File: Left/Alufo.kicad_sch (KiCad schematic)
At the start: 27 parts, among them J1 USB_C_Receptacle_USB2.0_16P_2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, J3 USB_C_Receptacle_USB2.0_16P_2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, SW10 BOOT, U1 CH552T, U3 USBLC6-2P6, U5 USBLC6-2P6

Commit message: Remove status LED resistor
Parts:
- removed R9: 470R, Resistor_SMD:R_0805_2012Metric, symbol Device:R
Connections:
- net LED: now also L1.3 (DIN)
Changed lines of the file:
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@@
 	(wire
 		(pts
-			(xy 55.88 220.98) (xy 59.69 220.98)
-		)
-		(stroke
-			(width 0)
-			(type default)
-		)
-	)
-	(wire
-		(pts
 			(xy 132.08 43.18) (xy 134.62 43.18)
 		)
@@
 	(wire
 		(pts
-			(xy 67.31 220.98) (xy 69.85 220.98)
-		)
-		(stroke
-			(width 0)
-			(type default)
-		)
-	)
-	(wire
-		(pts
 			(xy 60.96 48.26) (xy 62.23 48.26)
 		)
@@
 	(global_label "LED"
 		(shape input)
-		(at 55.88 220.98 180)
+		(at 69.85 220.98 180)
 		(fields_autoplaced yes)
 		(effects
@@
 		)
 		(property "Intersheetrefs" "${INTERSHEET_REFS}"
-			(at 49.4477 220.98 0)
+			(at 63.4177 220.98 0)
 			(effects
 				(font
@@
 					(unit 1)
 				)
-			)
-		)
-	)
-	(symbol
-		(lib_id "Device:R")
-		(at 63.5 220.98 90)
-		(unit 1)
-		(exclude_from_sim no)
-		(in_bom yes)
-		(on_board yes)
-		(dnp no)
-		(property "Reference" "R9"
-			(at 63.5 216.408 90)
-			(effects
-				(font
-					(size 1.27 1.27)
-				)
-			)
-		)
-		(property "Value" "470R"
-			(at 63.5 218.948 90)
-			(effects
-				(font
-					(size 1.27 1.27)
-				)
-			)
-		)
-		(property "Footprint" "Resistor_SMD:R_0805_2012Metric"
-			(at 63.5 222.758 90)
-			(effects
-				(font
-					(size 1.27 1.27)
-				)
-				(hide yes)
-			)
-		)
-		(property "Datasheet" "~"
-			(at 63.5 220.98 0)
-			(effects
-				(font
-					(size 1.27 1.27)
-				)
-				(hide yes)
-			)
-		)
-		(property "Description" ""
-			(at 63.5 220.98 0)
-			(effects
-				(font
-					(size 1.27 1.27)
-				)
-				(hide yes)
-			)
-		)
-		(property "LCSC" "C23186"
-			(at 63.5 220.98 90)
-			(effects
-				(font
-					(size 1.27 1.27)
-				)
-				(hide yes)
-			)
-		)
-		(property "DigiKey" "311-5.10KHR"
-			(at 63.5 220.98 90)
-			(effects
-				(font
-					(size 1.27 1.27)
-				)
-				(hide yes)
-			)
-		)
-		(pin "1"
-		)
-		(pin "2"
-		)
-		(instances
-			(project "Alufo"
-				(path "/52f043ac-ccff-4c85-bc10-2db9d3c9e3f3"
-					(reference "R9")
-					(unit 1)
-				)

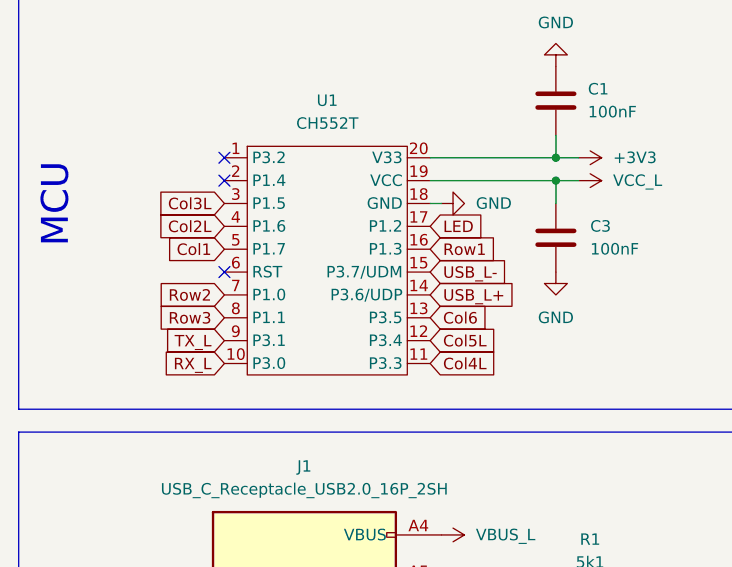
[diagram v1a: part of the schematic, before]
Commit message: Remove “L” from column labels
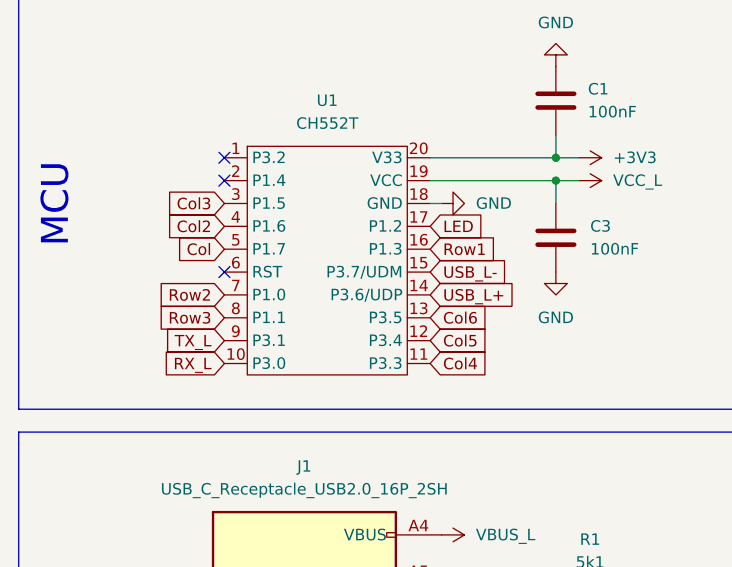
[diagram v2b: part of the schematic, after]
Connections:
- net Col1 renamed Col
- net Col2L renamed Col2
- net Col3L renamed Col3
- net Col4L renamed Col4
- net Col5L renamed Col5
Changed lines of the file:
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@@
 		)
 	)
-	(global_label "Col1"
+	(global_label "Col"
 		(shape input)
 		(at 38.1 53.34 180)
@@
 		)
 		(property "Intersheetrefs" "${INTERSHEET_REFS}"
-			(at 30.8211 53.34 0)
+			(at 32.0306 53.34 0)
 			(effects
 				(font
@@
 		)
 	)
-	(global_label "Col5L"
+	(global_label "Col5"
 		(shape input)
 		(at 60.96 63.5 0)
@@
 		)
 		(property "Intersheetrefs" "${INTERSHEET_REFS}"
-			(at 69.267 63.5 0)
+			(at 68.2389 63.5 0)
 			(effects
 				(font
@@
 		)
 	)
-	(global_label "Col3L"
+	(global_label "Col3"
 		(shape input)
 		(at 38.1 48.26 180)
@@
 		)
 		(property "Intersheetrefs" "${INTERSHEET_REFS}"
-			(at 29.793 48.26 0)
-			(effects
-				(font
-					(size 1.27 1.27)
-				)
-				(justify right)
-				(hide yes)
-			)
-		)
-	)
-	(global_label "Col2L"
+			(at 30.8211 48.26 0)
+			(effects
+				(font
+					(size 1.27 1.27)
+				)
+				(justify right)
+				(hide yes)
+			)
+		)
+	)
+	(global_label "Col2"
 		(shape input)
 		(at 38.1 50.8 180)
@@
 		)
 		(property "Intersheetrefs" "${INTERSHEET_REFS}"
-			(at 29.793 50.8 0)
+			(at 30.8211 50.8 0)
 			(effects
 				(font
@@
 		)
 	)
-	(global_label "Col4L"
+	(global_label "Col4"
 		(shape input)
 		(at 60.96 66.04 0)
@@
 		)
 		(property "Intersheetrefs" "${INTERSHEET_REFS}"
-			(at 69.267 66.04 0)
-			(effects
-				(font
+			(at 68.2389 66.04 0)
+			(effects
+				(font

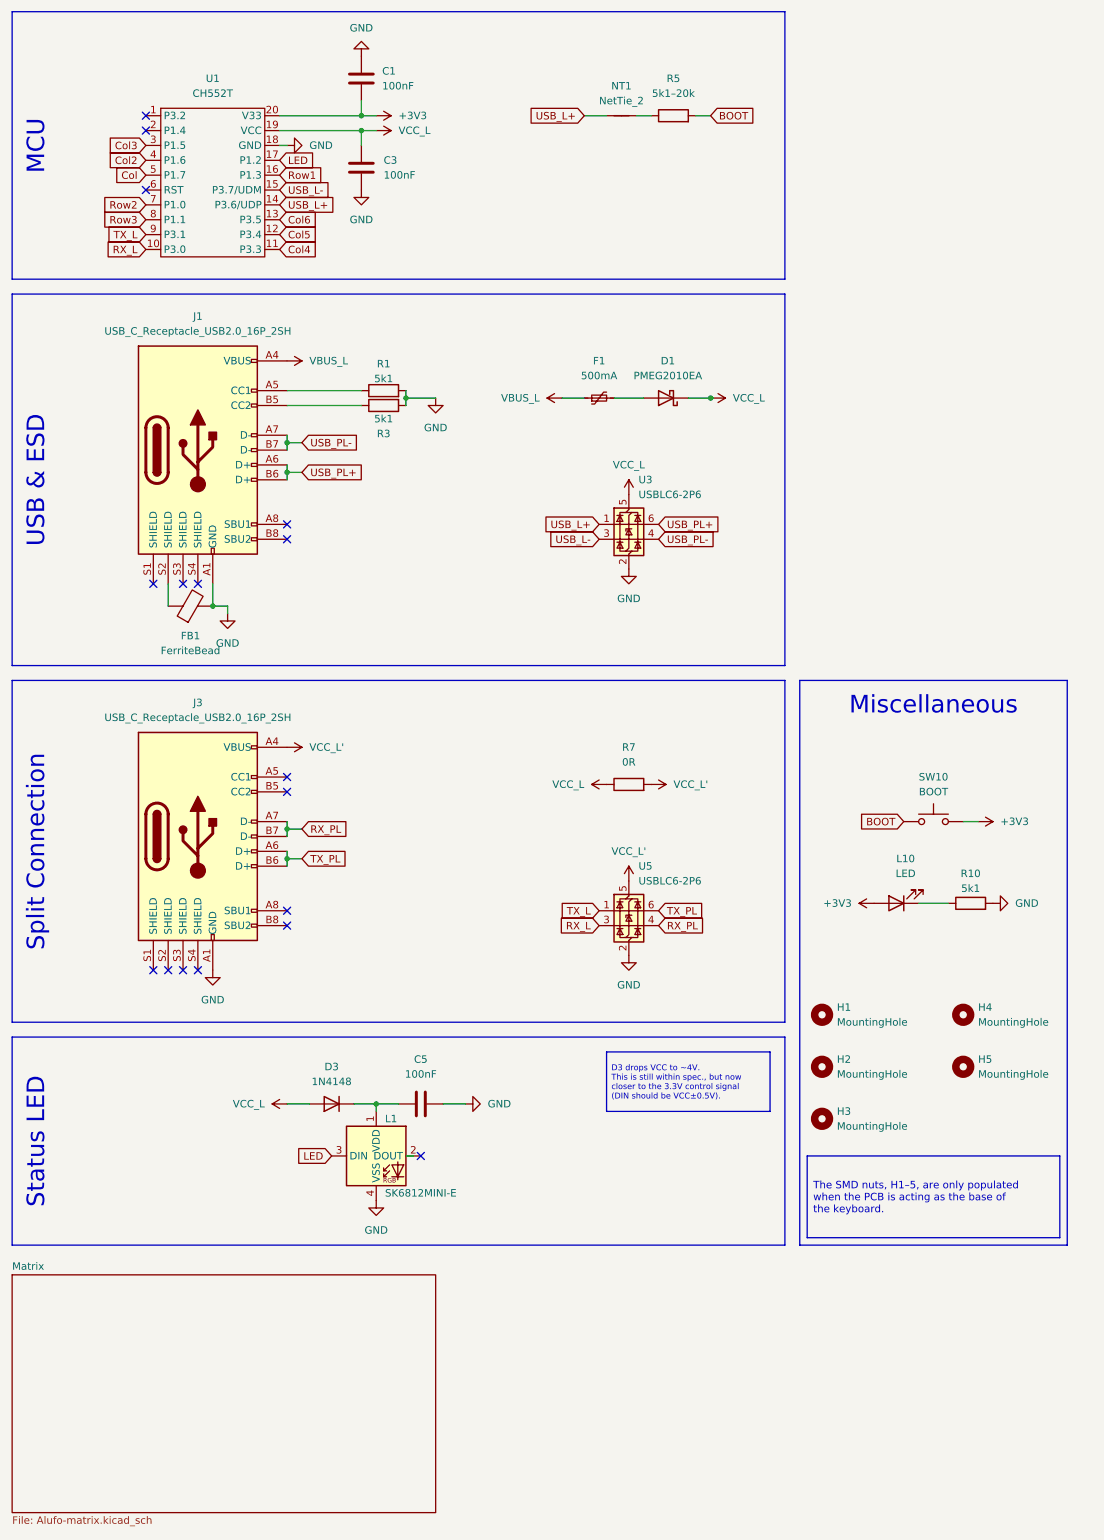
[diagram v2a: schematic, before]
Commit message: Remove “L” and “R” from all labels
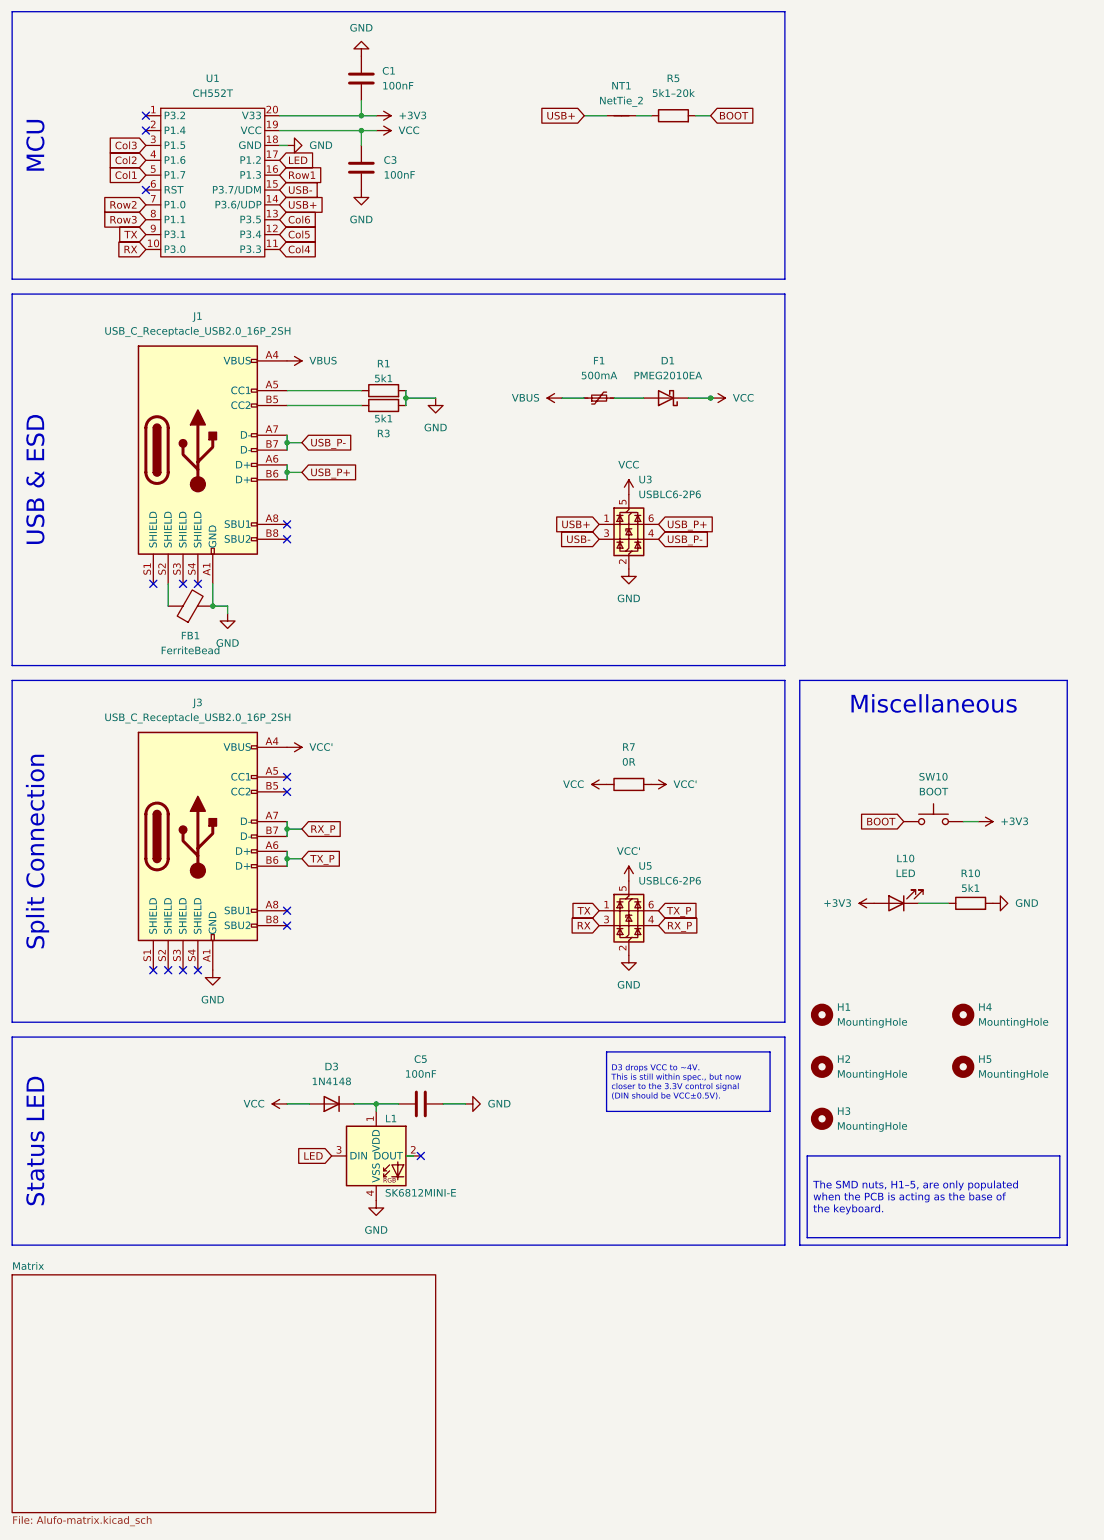
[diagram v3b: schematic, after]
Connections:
- net Col renamed Col1
- net RX_L renamed RX
- net RX_PL renamed RX_P
- net TX_L renamed TX
- net TX_PL renamed TX_P
- net USB_L+ renamed USB+
- net USB_L- renamed USB-
- net USB_PL+ renamed USB_P+
- net USB_PL- renamed USB_P-
- net VBUS_L renamed VBUS
- net VCC_L renamed VCC
- net VCC_L' renamed VCC'
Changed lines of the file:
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@@
 		)
 	)
-	(global_label "USB_L-"
+	(global_label "USB-"
 		(shape input)
 		(at 115.57 115.57 180)
@@
 		)
 		(property "Intersheetrefs" "${INTERSHEET_REFS}"
-			(at 105.2067 115.57 0)
+			(at 107.2024 115.57 0)
 			(effects
 				(font
@@
 		)
 	)
-	(global_label "USB_L+"
+	(global_label "USB+"
 		(shape input)
 		(at 115.57 113.03 180)
@@
 		)
 		(property "Intersheetrefs" "${INTERSHEET_REFS}"
-			(at 105.2067 113.03 0)
+			(at 107.2024 113.03 0)
 			(effects
 				(font
@@
 		)
 	)
-	(global_label "Col"
+	(global_label "Col1"
 		(shape input)
 		(at 38.1 53.34 180)
@@
 		)
 		(property "Intersheetrefs" "${INTERSHEET_REFS}"
-			(at 32.0306 53.34 0)
+			(at 30.8211 53.34 0)
 			(effects
 				(font
@@
 		)
 	)
-	(global_label "TX_PL"
+	(global_label "TX_P"
 		(shape input)
 		(at 125.73 179.07 0)
@@
 		)
 		(property "Intersheetrefs" "${INTERSHEET_REFS}"
-			(at 134.158 179.07 0)
+			(at 133.1299 179.07 0)
 			(effects
 				(font
@@
 		)
 	)
-	(global_label "USB_L+"
+	(global_label "USB+"
 		(shape input)
 		(at 60.96 58.42 0)
@@
 		)
 		(property "Intersheetrefs" "${INTERSHEET_REFS}"
-			(at 71.3233 58.42 0)
+			(at 69.3276 58.42 0)
 			(effects
 				(font
@@
 		)
 	)
-	(global_label "USB_PL-"
+	(global_label "USB_P-"
 		(shape input)
 		(at 125.73 115.57 0)
@@
 		)
 		(property "Intersheetrefs" "${INTERSHEET_REFS}"
-			(at 137.3633 115.57 0)
+			(at 136.3352 115.57 0)
 			(effects
 				(font
@@
 		)
 	)
-	(global_label "RX_PL"
+	(global_label "RX_P"
 		(shape input)
 		(at 64.77 165.1 0)
@@
 		)
 		(property "Intersheetrefs" "${INTERSHEET_REFS}"
-			(at 73.5004 165.1 0)
+			(at 72.4723 165.1 0)
 			(effects
 				(font
@@
 		)
 	)
-	(global_label "USB_PL-"
+	(global_label "USB_P-"
 		(shape input)
 		(at 64.77 99.06 0)
@@
 		)
 		(property "Intersheetrefs" "${INTERSHEET_REFS}"
-			(at 76.4033 99.06 0)
+			(at 75.3752 99.06 0)
 			(effects
 				(font
@@
 		)
 	)
-	(global_label "USB_PL+"
+	(global_label "USB_P+"
 		(shape input)
 		(at 125.73 113.03 0)
@@
 		)
 		(property "Intersheetrefs" "${INTERSHEET_REFS}"
-			(at 137.3633 113.03 0)
+			(at 136.3352 113.03 0)
 			(effects
 				(font
@@
 		)
 	)
-	(global_label "TX_L"
+	(global_label "TX"
 		(shape input)
 		(at 38.1 63.5 180)
@@
 		)
 		(property "Intersheetrefs" "${INTERSHEET_REFS}"
-			(at 30.942 63.5 0)
+			(at 32.9377 63.5 0)
 			(effects
 				(font
@@
 		)
 	)
-	(global_label "USB_L+"
+	(global_label "USB+"
 		(shape input)
 		(at 113.03 43.18 180)
@@
 		)
 		(property "Intersheetrefs" "${INTERSHEET_REFS}"
-			(at 102.6667 43.18 0)
+			(at 104.6624 43.18 0)
 			(effects
 				(font
@@
 		)
 	)
-	(global_label "RX_L"
+	(global_label "RX"
 		(shape input)
 		(at 115.57 181.61 180)
@@
 		)
 		(property "Intersheetrefs" "${INTERSHEET_REFS}"
-			(at 108.1096 181.61 0)
+			(at 110.1053 181.61 0)
 			(effects
 				(font
@@
 		)
 	)
-	(global_label "TX_L"
+	(global_label "TX"
 		(shape input)
 		(at 115.57 179.07 180)
@@
 		)
 		(property "Intersheetrefs" "${INTERSHEET_REFS}"
-			(at 108.412 179.07 0)
+			(at 110.4077 179.07 0)
 			(effects
 				(font
@@
 		)
 	)
-	(global_label "USB_PL+"
+	(global_label "USB_P+"
 		(shape input)
 		(at 64.77 104.14 0)
@@
 		)
 		(property "Intersheetrefs" "${INTERSHEET_REFS}"
-			(at 76.4033 104.14 0)
+			(at 75.3752 104.14 0)
 			(effects
 				(font
@@
 		)
 	)
-	(global_label "USB_L-"
+	(global_label "USB-"
 		(shape input)
 		(at 60.96 55.88 0)
@@
 		)
 		(property "Intersheetrefs" "${INTERSHEET_REFS}"
-			(at 71.3233 55.88 0)
+			(at 69.3276 55.88 0)
 			(effects
 				(font
@@
 		)
 	)
-	(global_label "TX_PL"
+	(global_label "TX_P"
 		(shape input)
 		(at 64.77 170.18 0)
@@
 		)
 		(property "Intersheetrefs" "${INTERSHEET_REFS}"
-			(at 73.198 170.18 0)
+			(at 72.1699 170.18 0)
 			(effects
 				(font
@@
 		)
 	)
-	(global_label "RX_L"
+	(global_label "RX"
 		(shape input)
 		(at 38.1 66.04 180)
@@
 		)
 		(property "Intersheetrefs" "${INTERSHEET_REFS}"
-			(at 30.6396 66.04 0)
+			(at 32.6353 66.04 0)
 			(effects
 				(font
@@
 		)
 	)
-	(global_label "RX_PL"
+	(global_label "RX_P"
 		(shape input)
 		(at 125.73 181.61 0)
@@
 		)
 		(property "Intersheetrefs" "${INTERSHEET_REFS}"
-			(at 134.4604 181.61 0)
+			(at 133.4323 181.61 0)
 			(effects
 				(font
@@
 			)
 		)
-		(property "Value" "VBUS_L"
+		(property "Value" "VBUS"
 			(at 105.41 91.4399 90)
 			(effects
@@
 			)
 		)
-		(property "Value" "VCC_L'"
+		(property "Value" "VCC'"
 			(at 66.04 151.1299 90)
 			(effects
@@
 			)
 		)
-		(property "Value" "VCC_L'"
+		(property "Value" "VCC'"
 			(at 120.65 168.91 0)
 			(effects
@@
 			)
 		)
-		(property "Value" "VBUS_L"
+		(property "Value" "VBUS"
 			(at 66.04 85.0899 90)
 			(effects
@@
 			)
 		)
-		(property "Value" "VCC_L'"
+		(property "Value" "VCC'"
 			(at 128.27 157.4799 90)
 			(effects
@@
 			)
 		)
-		(property "Value" "VCC_L"
+		(property "Value" "VCC"
 			(at 138.43 91.4399 90)
 			(effects
@@
 			)
 		)
-		(property "Value" "VCC_L"
+		(property "Value" "VCC"
 			(at 120.65 102.87 0)
 			(effects
@@
 			)
 		)
-		(property "Value" "VCC_L"
+		(property "Value" "VCC"
 			(at 58.42 212.0899 90)
 			(effects
@@
 			)
 		)
-		(property "Value" "VCC_L"
+		(property "Value" "VCC"
 			(at 113.03 157.4799 90)
 			(effects
@@
 			)
 		)
-		(property "Value" "VCC_L"
+		(property "Value" "VCC"
 			(at 81.28 45.7199 90)
 			(effects
